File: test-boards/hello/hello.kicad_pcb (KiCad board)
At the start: 2 copper layers, 20 x 20 mm, 2 parts, among them J1 Conn_01x02_Pin

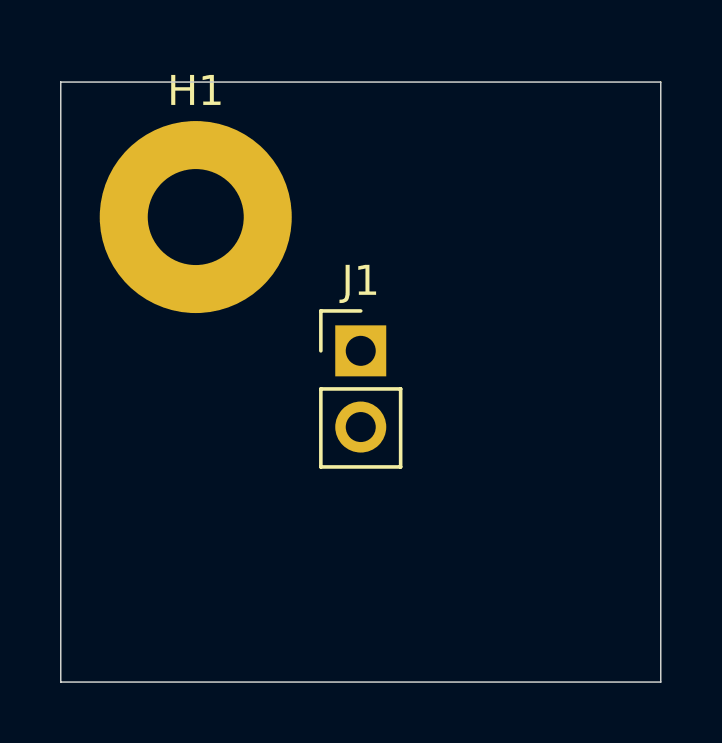
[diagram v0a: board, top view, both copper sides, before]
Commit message: hello test board with components on both sides
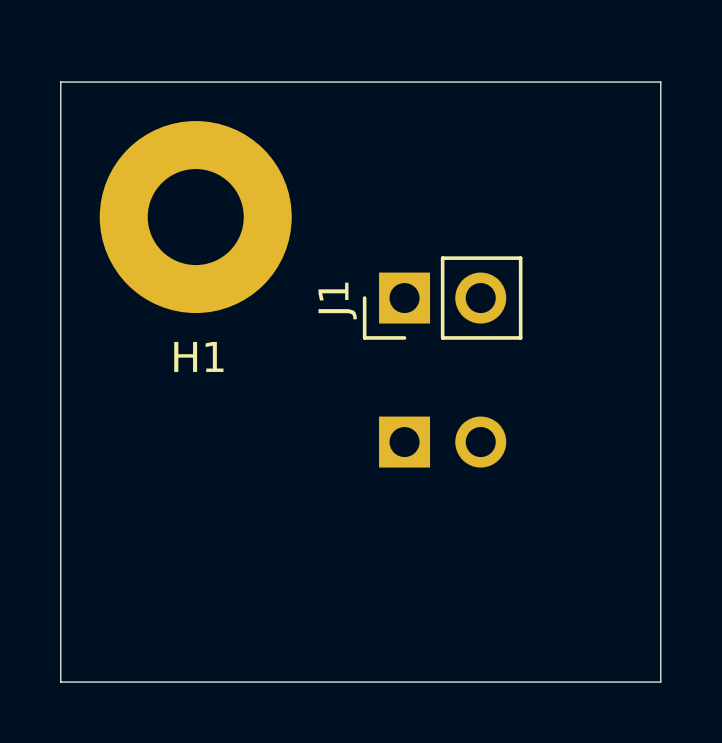
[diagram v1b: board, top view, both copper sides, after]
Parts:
- added J2: Conn_01x02_Pin, Connector_PinHeader_2.54mm:PinHeader_1x02_P2.54mm_Vertical, B.Cu at (61.5, 62.0)
- moved J1 2.29 mm to (61.5, 57.2), turned to 90 degrees
